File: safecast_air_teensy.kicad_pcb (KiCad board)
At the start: 2 copper layers, 108 x 69.8 mm, 22 parts, among them P1 CONN_5X2, P2 CONN_5X2, P3 CONN_7X2, P4 CONN_2X2, P5 CONN_2, P6 CONN_2, P7 CONN_2, P8 CONN_3X2, P9 CONN_2, U1 GPS, U2 XBEE, U3 LCD, U4 OPENLOG, U5 POLOLU_3V3, U6 TEENSY3.1, U7 R5_BUSSED

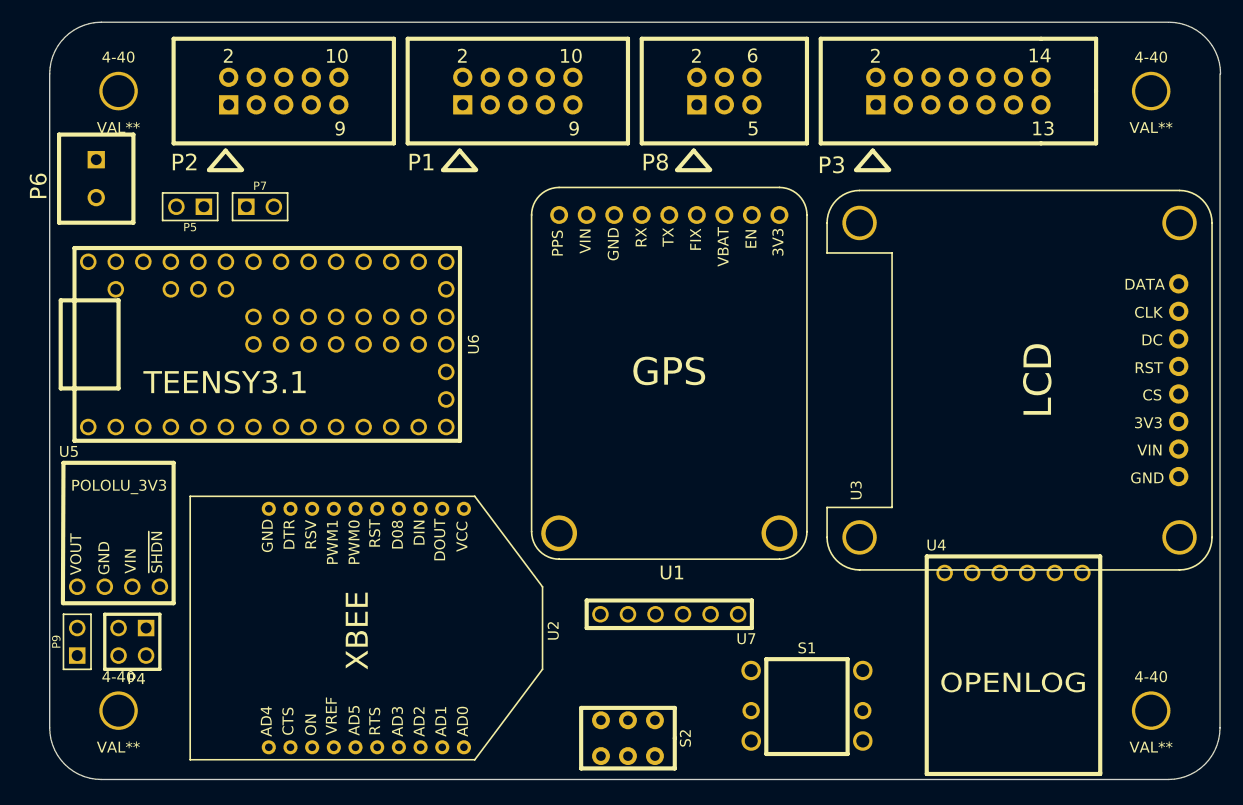
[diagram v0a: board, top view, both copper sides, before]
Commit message: Finished initial PCB routing.
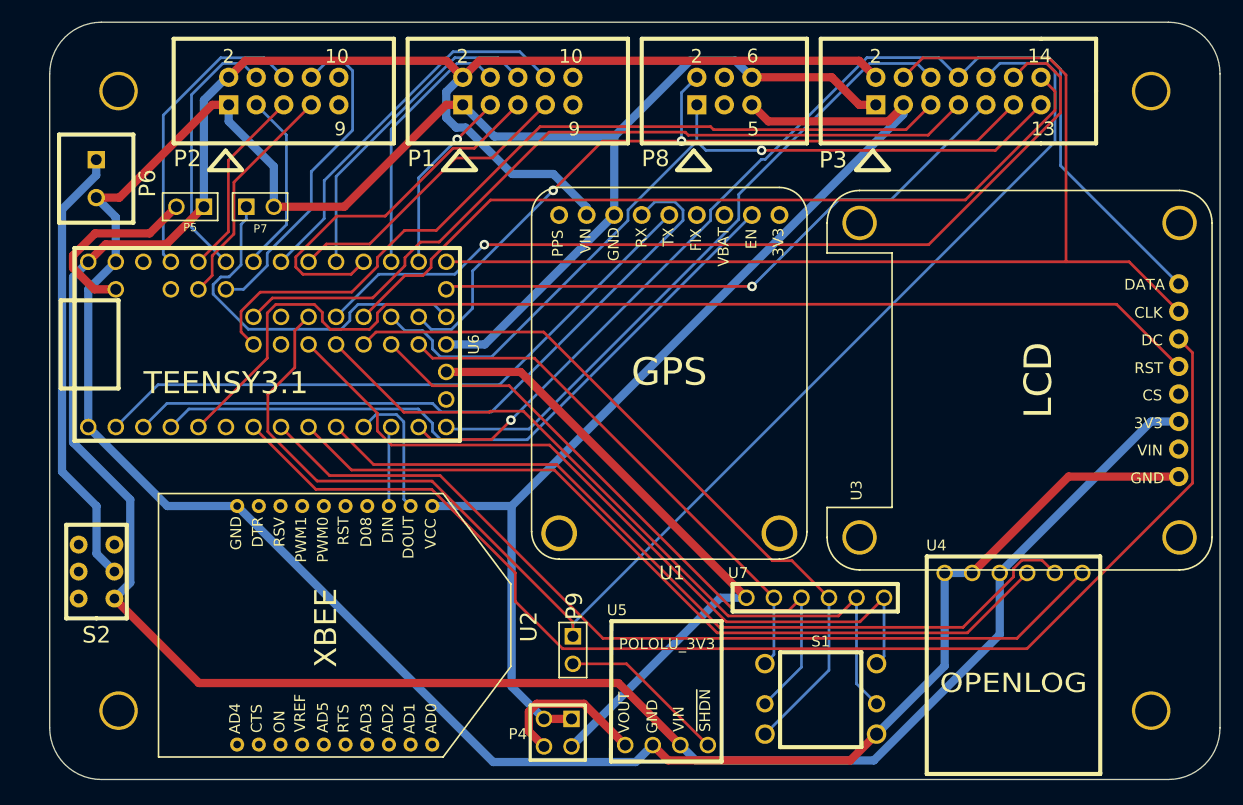
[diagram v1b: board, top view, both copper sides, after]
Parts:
- moved U5 52.6 mm to (82.3, 92.1)
- moved S2 51.4 mm to (29.7, 76.1), turned to 180 degrees
- moved P9 45.7 mm to (73.7, 83.3), turned to 270 degrees
- moved P4 40.1 mm to (72.3, 90.9)
- moved U7 13.5 mm to (96.0, 78.5), turned to 0 degrees
- moved U2 2.93 mm to (51.7, 81.0)
- moved S1 1.42 mm to (96.5, 88.3)
- renumbered 4-40 to H1, 4-40 to H2, 4-40 to H3, 4-40 to H4
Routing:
- net GND: track 0.00 -> 273.2 mm
- net /5V: track 0.00 -> 264.6 mm
- net /D33: track 0.00 -> 126.6 mm
- net /LCD_DC: track 0.00 -> 116.8 mm
- net /SCK: track 0.00 -> 103.1 mm
- net /LCD_CS: track 0.00 -> 102.8 mm
- net /MOSI: track 0.00 -> 101.1 mm, vias 0 -> 1
- net /3V3: track 0.00 -> 98.0 mm
- net /LOG_GRN: track 0.00 -> 84.5 mm
- net /D32: track 0.00 -> 83.3 mm, vias 0 -> 1
- net /LOG_RXI: track 0.00 -> 77.5 mm
- net /LOG_TXO: track 0.00 -> 76.4 mm
- net /D30: track 0.00 -> 76.2 mm, vias 0 -> 1
- net /A12: track 0.00 -> 75.8 mm
- net /D31: track 0.00 -> 75.7 mm
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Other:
- net class Pwr added: clearance 0.254, trace_width 0.762, via_dia 0.889, via_drill 0.635

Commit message: Cleaned up silkscreen and added gerber files for version 0.1 revision 1.
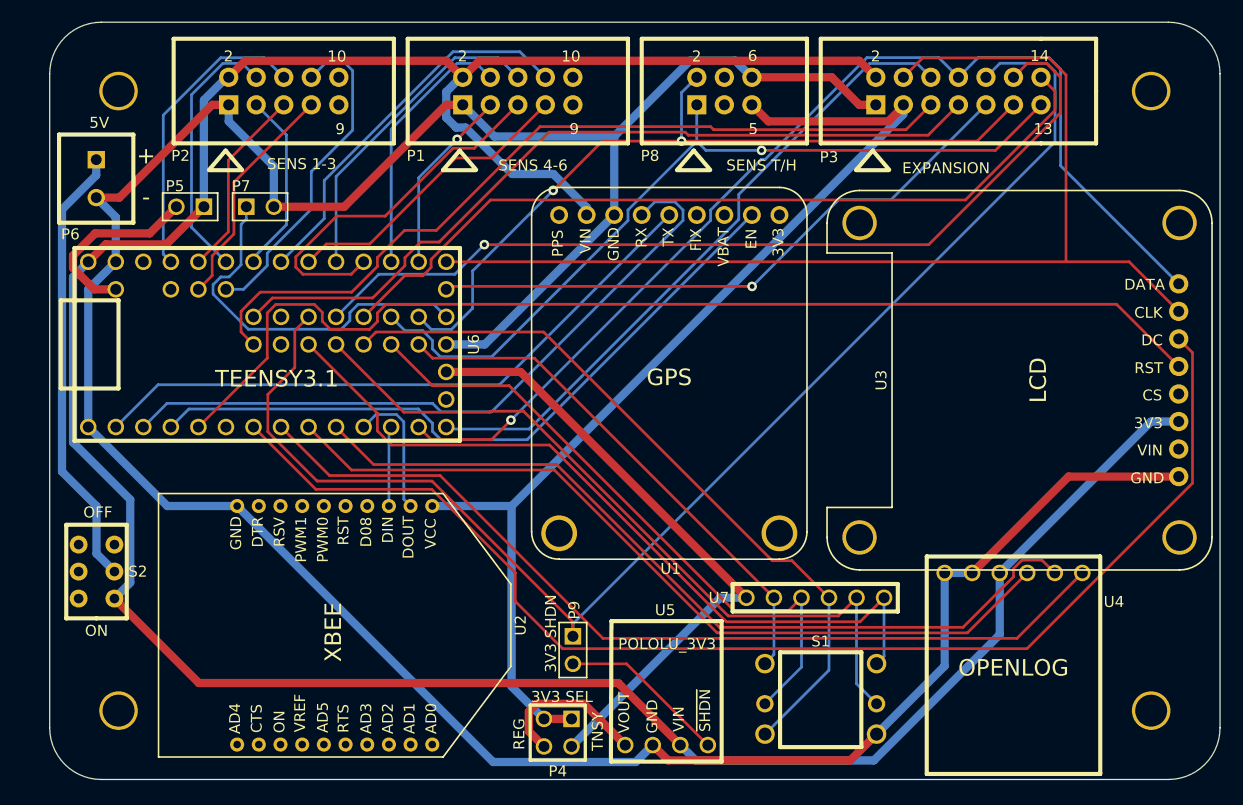
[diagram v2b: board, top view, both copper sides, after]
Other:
- board text added: "+"
- board text added: "-"
- board text added: "3V3 SEL"
- board text added: "3V3 SHDN"
- board text added: "5V"
- board text added: "EXPANSION"
- board text added: "OFF"
- board text added: "ON"
- board text added: "REG"
- board text added: "SENS 1-3"
- board text added: "SENS 4-6"
- board text added: "SENS T/H"
- board text added: "Safecast Air Prototype V0.1 R1 www.iorodeo.com"
- board text added: "TNSY"
